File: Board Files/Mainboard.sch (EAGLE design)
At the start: 119 parts, among them J1 I2C Display

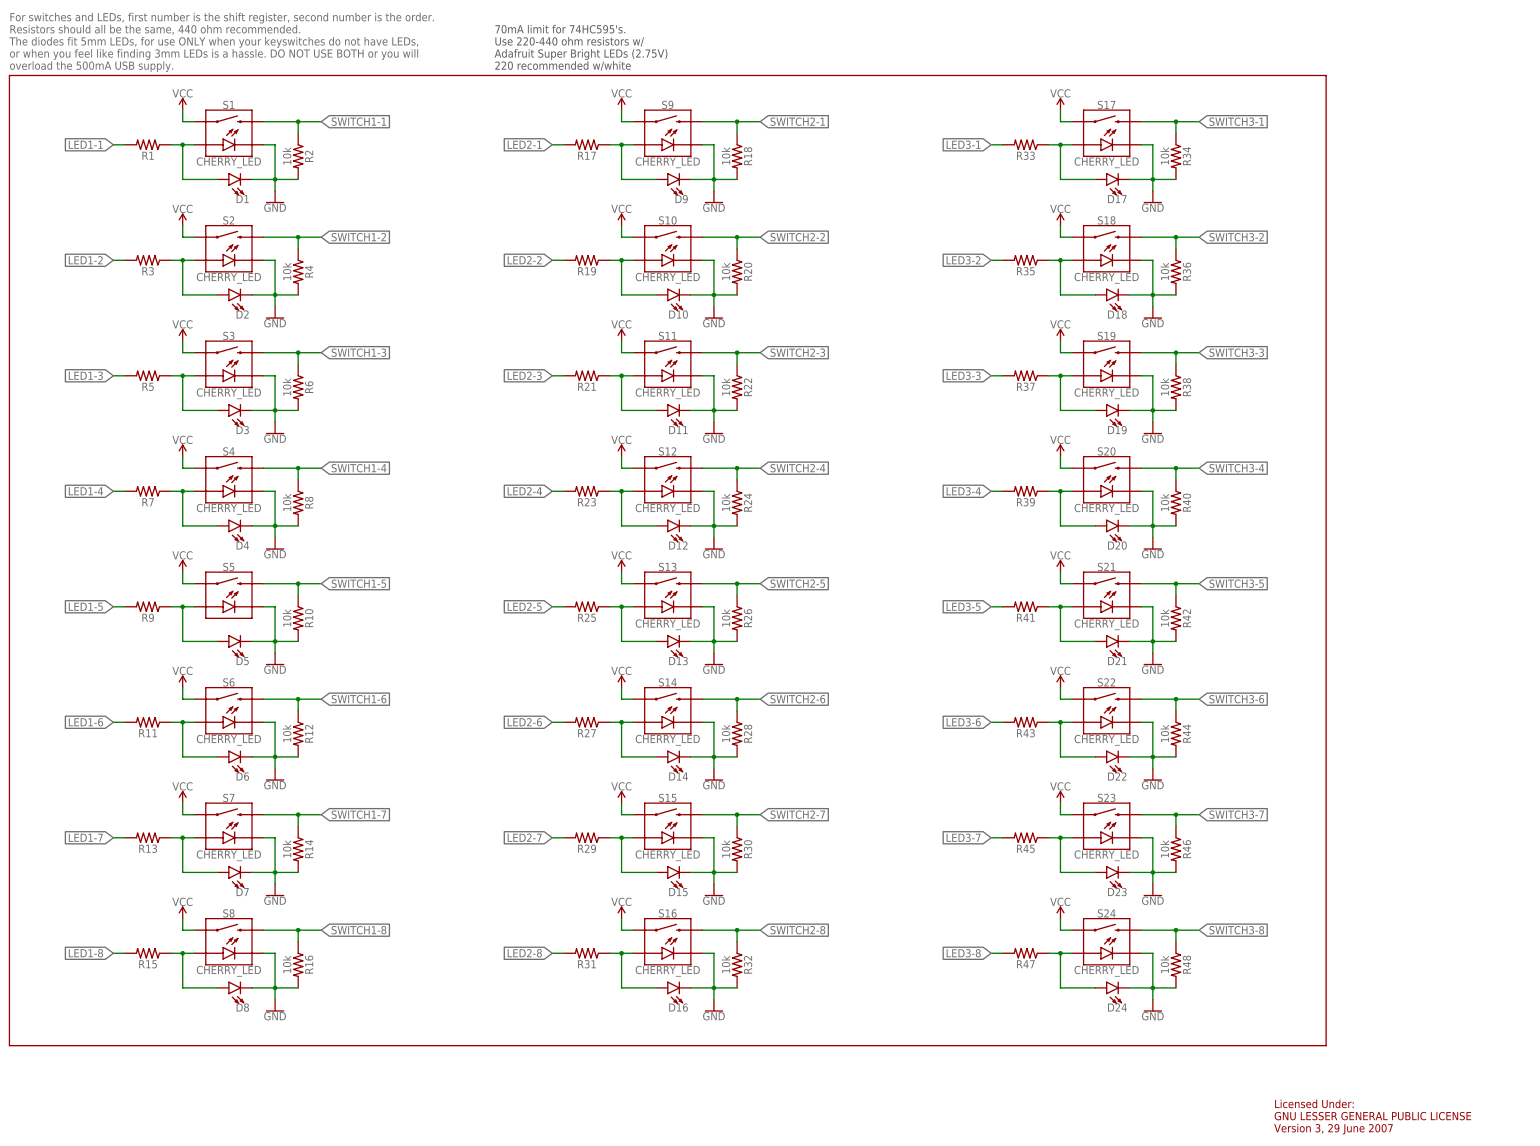
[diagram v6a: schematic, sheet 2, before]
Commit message: Updated Assembly and Board Tweaks
-Added color to parts in assembly, made renders
-Did final layout adjustments on mainboard. Renamed resistors
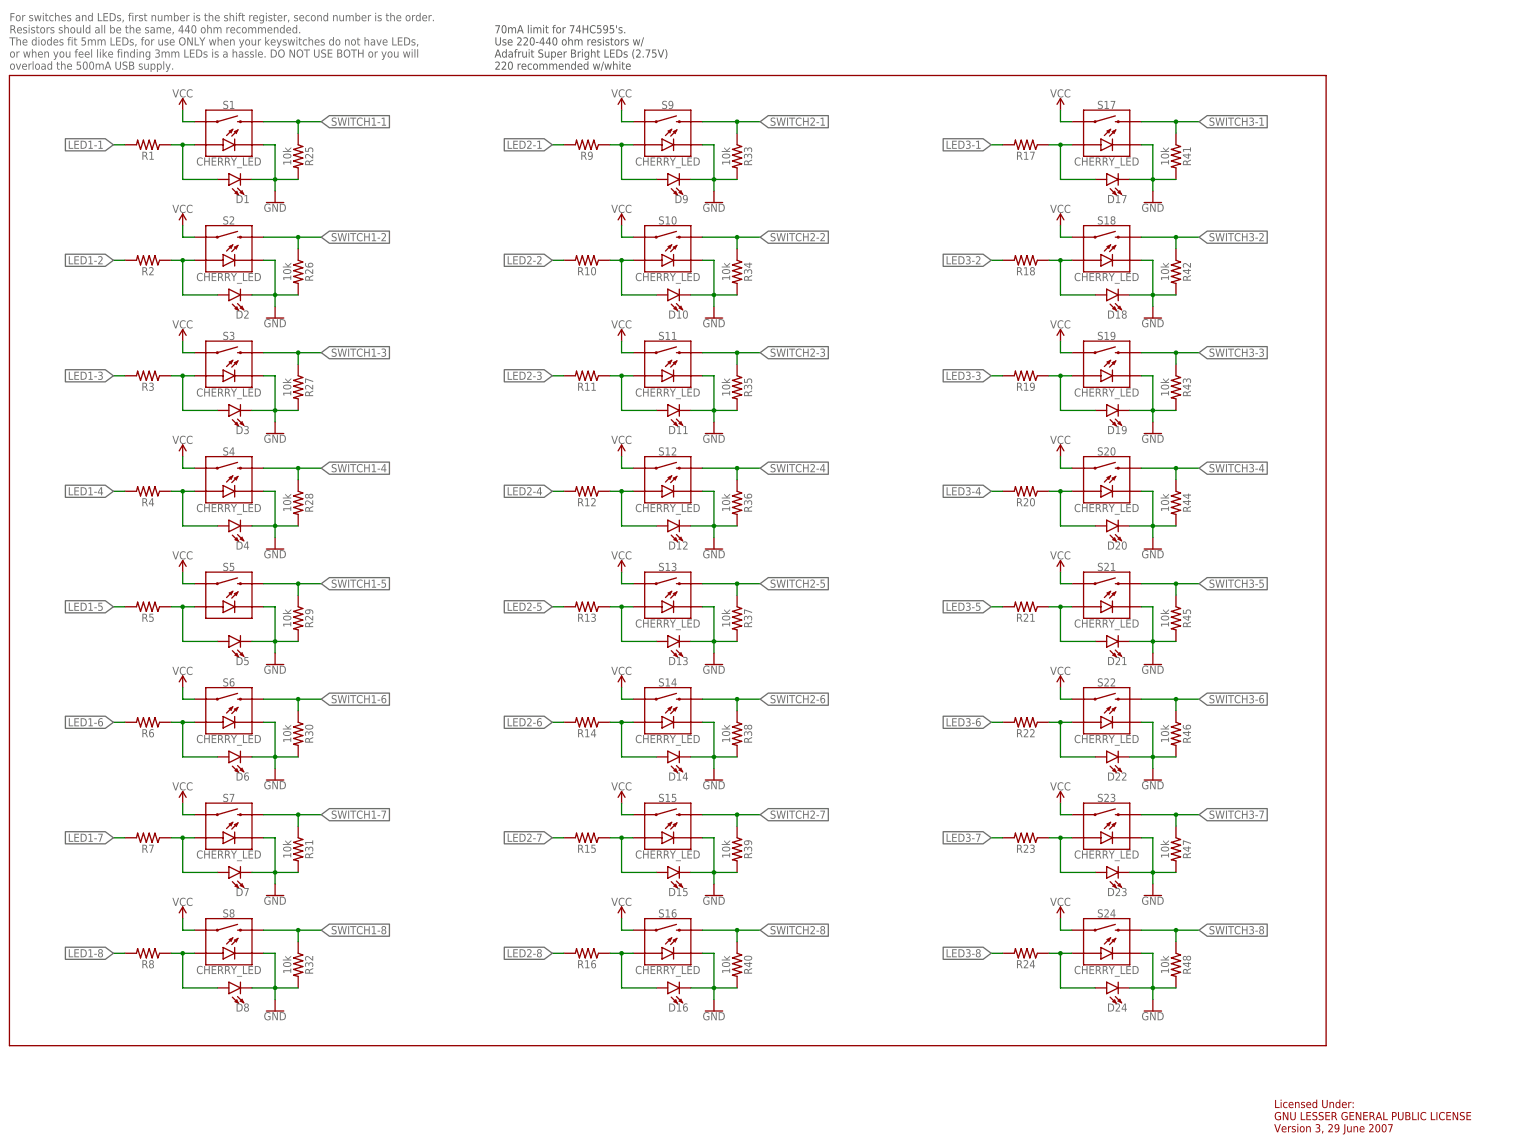
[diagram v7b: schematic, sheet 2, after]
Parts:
- R10, R12, R14, R16, R18, R2, R20, R22, R24, R4, R6, R8: value 10k -> (none); device SparkFun-Resistors:10KOHM-HORIZ-1/4W-1% -> SparkFun-Resistors:RESISTORAXIAL-0.3
- R25, R27, R29, R31, R33, R35, R37, R39, R41, R43, R45, R47: value (none) -> 10k; device SparkFun-Resistors:RESISTORAXIAL-0.3 -> SparkFun-Resistors:10KOHM-HORIZ-1/4W-1%
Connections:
- net GND: now also R25.2, R27.2, R29.2, R31.2, R33.2, R35.2, R37.2, R39.2, R41.2, R43.2, R45.2, R47.2; no longer R10.2, R12.2, R14.2, R16.2, R18.2, R2.2, R20.2, R22.2, R24.2, R4.2, R6.2, R8.2
- net LED1-2: now also R2.2; no longer R3.2
- net LED1-3: now also R3.2; no longer R5.2
- net LED1-4: now also R4.2; no longer R7.2
- net LED1-5: now also R5.2; no longer R9.2
- net LED1-6: now also R6.2; no longer R11.2
- net LED1-7: now also R7.2; no longer R13.2
- net LED1-8: now also R8.2; no longer R15.2
- net LED2-1: now also R9.2; no longer R17.2
- net LED2-2: now also R10.2; no longer R19.2
- net LED2-3: now also R11.2; no longer R21.2
- net LED2-4: now also R12.2; no longer R23.2
- net LED2-5: now also R13.2; no longer R25.2
- net LED2-6: now also R14.2; no longer R27.2
- net LED2-7: now also R15.2; no longer R29.2
- net LED2-8: now also R16.2; no longer R31.2
- net LED3-1: now also R17.2; no longer R33.2
- net LED3-2: now also R18.2; no longer R35.2
- net LED3-3: now also R19.2; no longer R37.2
- net LED3-4: now also R20.2; no longer R39.2
- net LED3-5: now also R21.2; no longer R41.2
- net LED3-6: now also R22.2; no longer R43.2
- net LED3-7: now also R23.2; no longer R45.2
- net LED3-8: now also R24.2; no longer R47.2
- net N$10: now also R10.1; no longer R19.1
- net N$11: now also R11.1; no longer R21.1
- net N$12: now also R12.1; no longer R23.1
- net N$13: now also R13.1; no longer R25.1
- net N$14: now also R14.1; no longer R27.1
- net N$15: now also R15.1; no longer R29.1
- net N$16: now also R16.1; no longer R31.1
- net N$17: now also R17.1; no longer R33.1
- net N$18: now also R18.1; no longer R35.1
- net N$19: now also R19.1; no longer R37.1
- net N$2: now also R2.1; no longer R3.1
- net N$20: now also R20.1; no longer R39.1
- net N$21: now also R21.1; no longer R41.1
- net N$22: now also R22.1; no longer R43.1
- net N$23: now also R23.1; no longer R45.1
- net N$24: now also R24.1; no longer R47.1
- net N$3: now also R3.1; no longer R5.1
- net N$4: now also R4.1; no longer R7.1
- net N$5: now also R5.1; no longer R9.1
- net N$6: now also R6.1; no longer R11.1
- net N$7: now also R7.1; no longer R13.1
- net N$8: now also R8.1; no longer R15.1
- net N$9: now also R9.1; no longer R17.1
- net SWITCH1-1: now also R25.1; no longer R2.1
- net SWITCH1-2: now also R26.1; no longer R4.1
- net SWITCH1-3: now also R27.1; no longer R6.1
- net SWITCH1-4: now also R28.1; no longer R8.1
- net SWITCH1-5: now also R29.1; no longer R10.1
- net SWITCH1-6: now also R30.1; no longer R12.1
- net SWITCH1-7: now also R31.1; no longer R14.1
- net SWITCH1-8: now also R32.1; no longer R16.1
- net SWITCH2-1: now also R33.1; no longer R18.1
- net SWITCH2-2: now also R34.1; no longer R20.1
- net SWITCH2-3: now also R35.1; no longer R22.1
- net SWITCH2-4: now also R36.1; no longer R24.1
- net SWITCH2-5: now also R37.1; no longer R26.1
- net SWITCH2-6: now also R38.1; no longer R28.1
- net SWITCH2-7: now also R39.1; no longer R30.1
- net SWITCH2-8: now also R40.1; no longer R32.1
- net SWITCH3-1: now also R41.1; no longer R34.1
- net SWITCH3-2: now also R42.1; no longer R36.1
- net SWITCH3-3: now also R43.1; no longer R38.1
- net SWITCH3-4: now also R44.1; no longer R40.1
- net SWITCH3-5: now also R45.1; no longer R42.1
- net SWITCH3-6: now also R46.1; no longer R44.1
- net SWITCH3-7: now also R47.1; no longer R46.1
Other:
- moved on the sheet: R10, R11, R12, R13, R14, R15, R16, R17, R18, R19, R2, R20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
